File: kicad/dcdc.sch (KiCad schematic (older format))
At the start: 48 parts, among them Q1 IPP045N10N3G, Q2 IPP045N10N3G, Q3 IPP045N10N3G, U1 LM5107, U3 INA186

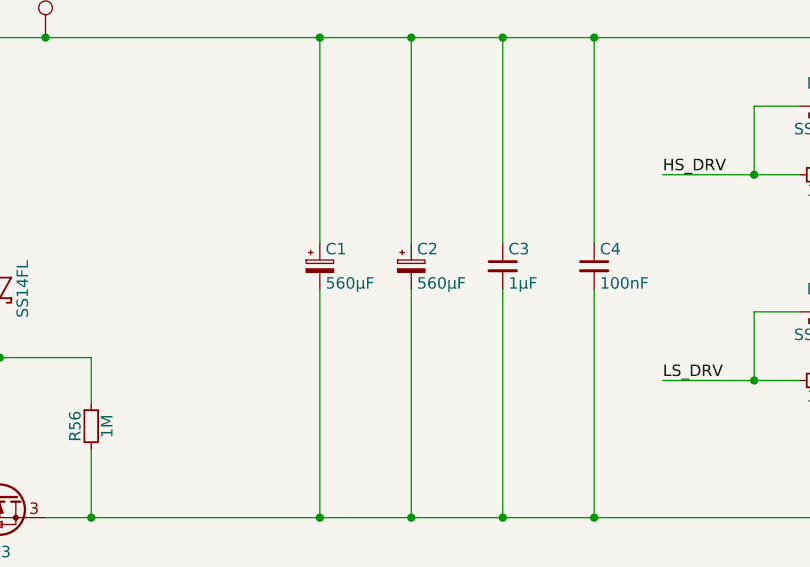
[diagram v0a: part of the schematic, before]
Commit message: Small updates in layout and documentation (v0.1.1)
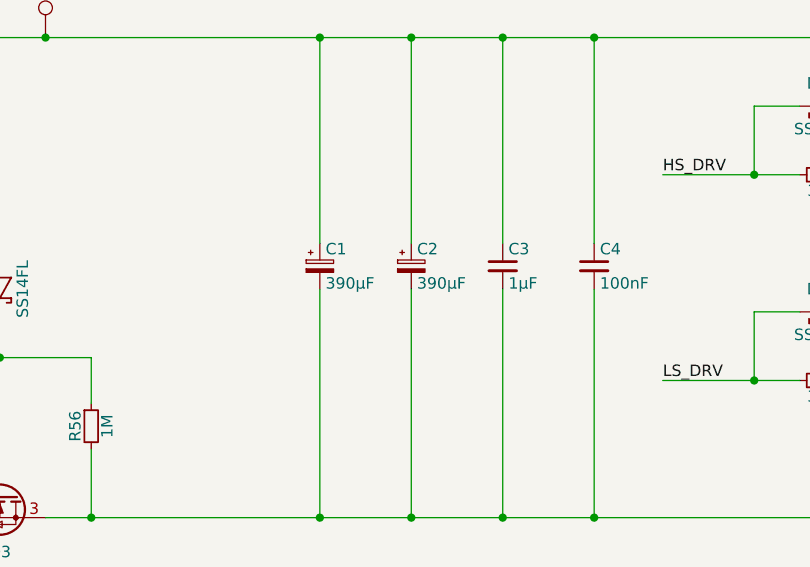
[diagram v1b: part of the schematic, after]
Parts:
- C1, C2: value 560µF -> 390µF; PartNumber EKZN101ELL561MM25S -> EKZN101ELL391MM20S; Remarks 100V, 2.27A, 18x25 -> 100V, 2.27A, 18x20
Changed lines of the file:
@@
 Sheet 2 6
 Title "MPPT 2420 HC"
-Date "2020-05-08"
-Rev "0.1"
+Date "2020-11-18"
+Rev "0.1.1"
 Comp "Libre Solar Technologies GmbH"
 Comment1 "Author: Martin Jäger"
@@
 P 4700 2500
 F 0 "C2" H 4725 2575 50  0000 L CNN
-F 1 "560µF" H 4725 2425 50  0000 L CNN
+F 1 "390µF" H 4725 2425 50  0000 L CNN
 F 2 "Capacitor_THT:CP_Radial_D18.0mm_P7.50mm" H 4725 2275 50  0001 L CNN
 F 3 "" H 4725 2575 50  0000 C CNN
 F 4 "United Chemi-Con" H 1300 700 50  0001 C CNN "Manufacturer"
-F 5 "EKZN101ELL561MM25S" H 1300 700 50  0001 C CNN "PartNumber"
-F 6 "100V, 2.27A, 18x25" H 700 400 60  0001 C CNN "Remarks"
+F 5 "EKZN101ELL391MM20S" H 1300 700 50  0001 C CNN "PartNumber"
+F 6 "100V, 2.27A, 18x20" H 700 400 60  0001 C CNN "Remarks"
 	1    4700 2500
 	1    0    0    -1
@@
 P 4300 2500
 F 0 "C1" H 4325 2575 50  0000 L CNN
-F 1 "560µF" H 4325 2425 50  0000 L CNN
+F 1 "390µF" H 4325 2425 50  0000 L CNN
 F 2 "Capacitor_THT:CP_Radial_D18.0mm_P7.50mm" H 4325 2275 50  0001 L CNN
 F 3 "" H 4325 2575 50  0000 C CNN
 F 4 "United Chemi-Con" H 900 700 50  0001 C CNN "Manufacturer"
-F 5 "EKZN101ELL561MM25S" H 900 700 50  0001 C CNN "PartNumber"
-F 6 "100V, 2.27A, 18x25" H 700 400 60  0001 C CNN "Remarks"
+F 5 "EKZN101ELL391MM20S" H 900 700 50  0001 C CNN "PartNumber"
+F 6 "100V, 2.27A, 18x20" H 700 400 60  0001 C CNN "Remarks"
 	1    4300 2500
 	1    0    0    -1

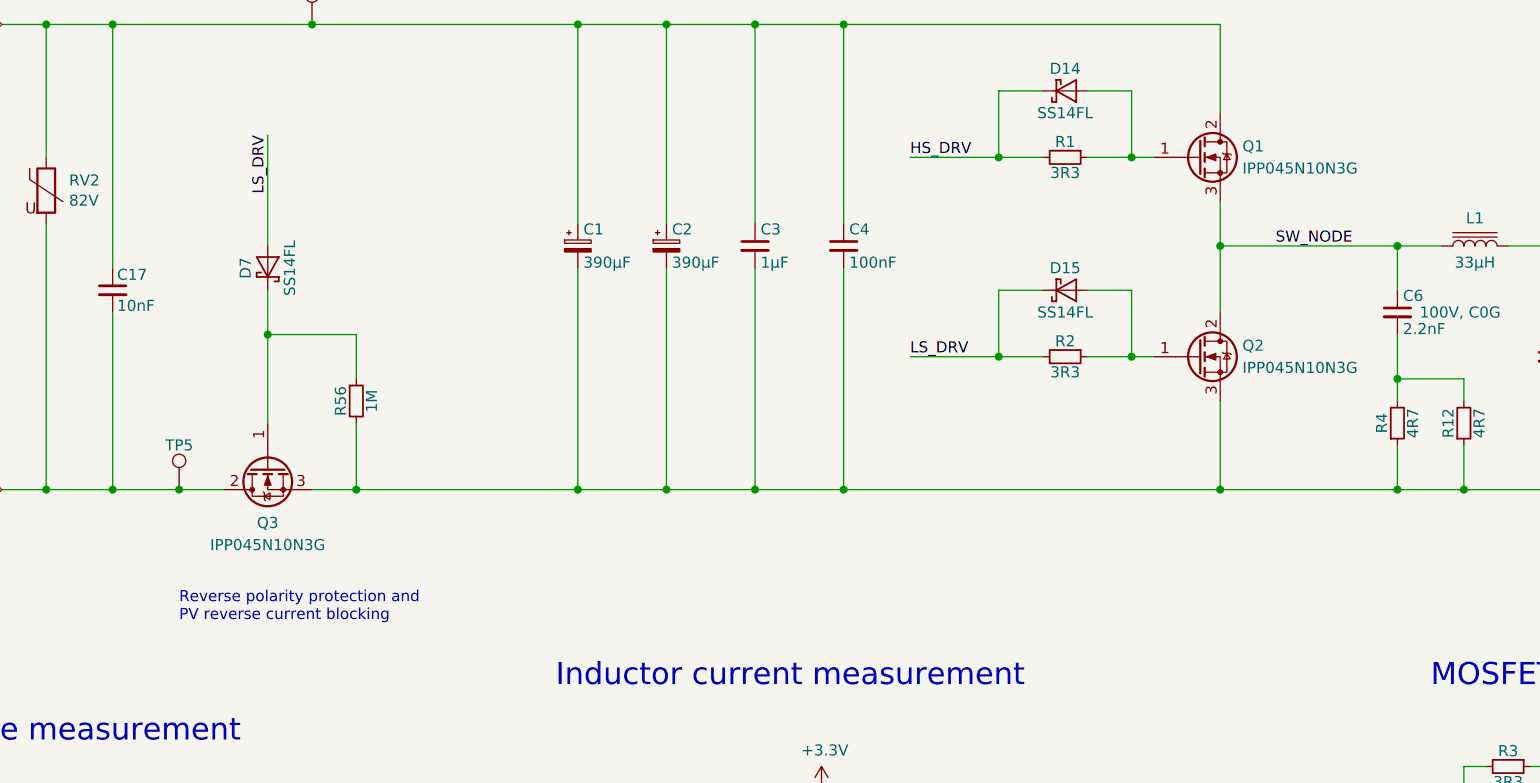
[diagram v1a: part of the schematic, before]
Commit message: Update to v0.2 with improvements after testing
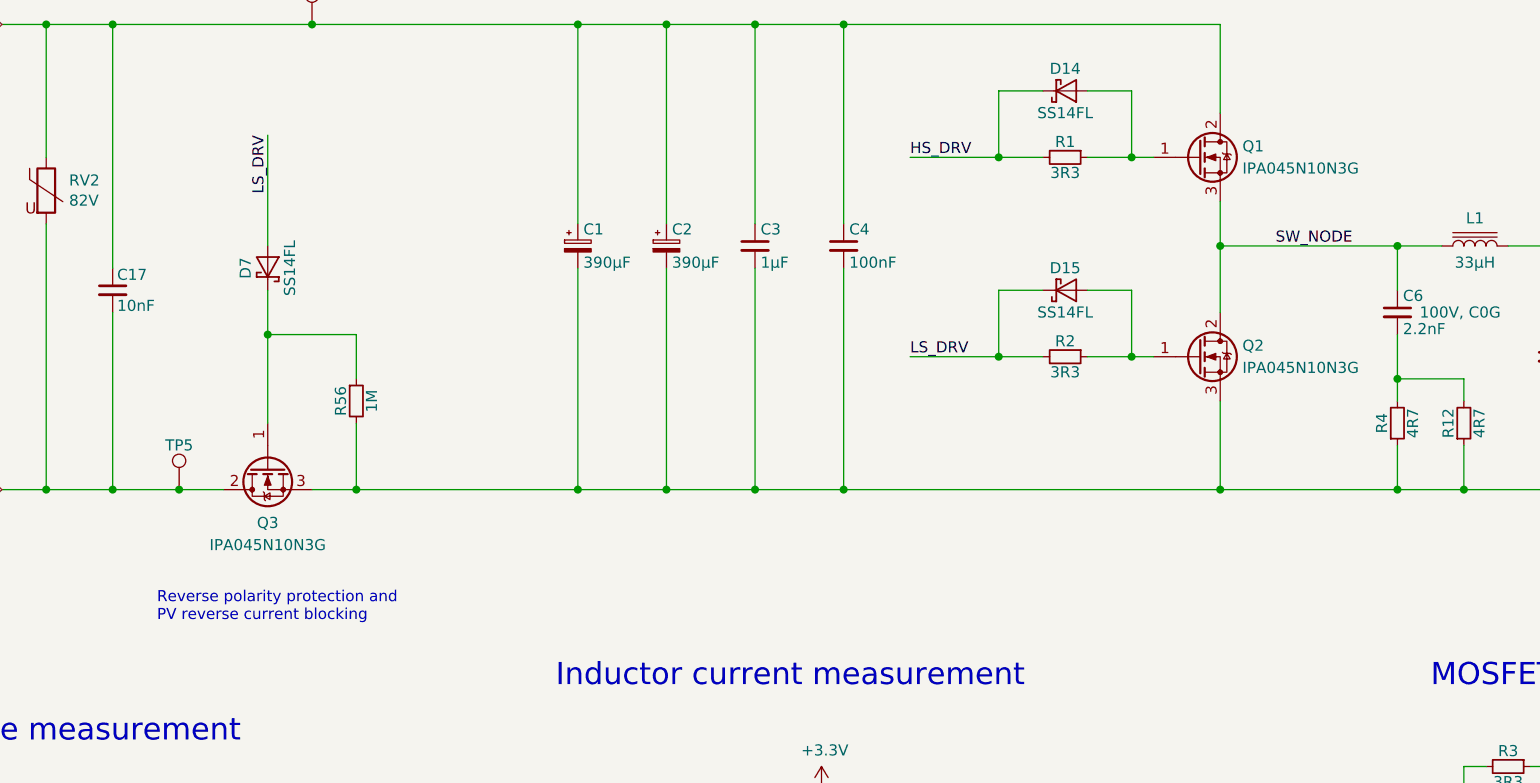
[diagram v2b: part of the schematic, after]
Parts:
- C42, C44: Manufacturer (none) -> EPCOS / TDK; PartNumber 224J63 -> B32529C224J; Remarks (none) -> Alternative: Kemet MMK5224K63J01L16.5TA18
- Q1, Q2, Q3: value IPP045N10N3G -> IPA045N10N3G; PartNumber IPP045N10N3G -> IPA045N10N3G; Remarks Alternative: IPA045N10N3G -> Alternative: IPP045N10N3G
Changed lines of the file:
@@
 Sheet 2 6
 Title "MPPT 2420 HC"
-Date "2020-11-18"
-Rev "0.1.1"
+Date "2020-12-11"
+Rev "0.2"
 Comp "Libre Solar Technologies GmbH"
-Comment1 "Author: Martin Jäger"
-Comment2 "Website: http://libre.solar"
-Comment3 ""
+Comment1 "https://libre.solar"
+Comment2 "Author: Martin Jäger"
+Comment3 "License: Creative Commons Attribution-ShareAlike 4.0 International"
 Comment4 ""
 $EndDescr
@@
 P 7100 2100
 F 0 "Q1" H 7300 2150 50  0000 L CNN
-F 1 "IPP045N10N3G" H 7300 2050 50  0000 L CNN
+F 1 "IPA045N10N3G" H 7300 2050 50  0000 L CNN
 F 2 "LibreSolar:TO-220-3_Horizontal_BottomHeatsink" H 7300 2200 50  0001 C CNN
 F 3 "" H 7100 2100 50  0001 C CNN
 F 4 "Infineon" H 1100 300 50  0001 C CNN "Manufacturer"
-F 5 "IPP045N10N3G" H 1100 300 50  0001 C CNN "PartNumber"
+F 5 "IPA045N10N3G" H 1100 300 50  0001 C CNN "PartNumber"
 F 6 "" H 7100 2100 50  0001 C CNN "Alternative"
-F 7 "Alternative: IPA045N10N3G" H 7100 2100 50  0001 C CNN "Remarks"
+F 7 "Alternative: IPP045N10N3G" H 7100 2100 50  0001 C CNN "Remarks"
 	1    7100 2100
 	1    0    0    -1
@@
 P 7100 3000
 F 0 "Q2" H 7300 3050 50  0000 L CNN
-F 1 "IPP045N10N3G" H 7300 2950 50  0000 L CNN
+F 1 "IPA045N10N3G" H 7300 2950 50  0000 L CNN
 F 2 "LibreSolar:TO-220-3_Horizontal_BottomHeatsink" H 7300 3100 50  0001 C CNN
 F 3 "" H 7100 3000 50  0001 C CNN
 F 4 "Infineon" H 1100 500 50  0001 C CNN "Manufacturer"
-F 5 "IPP045N10N3G" H 1100 500 50  0001 C CNN "PartNumber"
+F 5 "IPA045N10N3G" H 1100 500 50  0001 C CNN "PartNumber"
 F 6 "" H 7100 3000 50  0001 C CNN "Alternative"
-F 7 "Alternative: IPA045N10N3G" H 7100 3000 50  0001 C CNN "Remarks"
+F 7 "Alternative: IPP045N10N3G" H 7100 3000 50  0001 C CNN "Remarks"
 	1    7100 3000
 	1    0    0    -1
@@
 	2200 2800 2200 3600
 Connection ~ 2200 3600
-Text Notes 2500 4200 0    50   ~ 0
+Text Notes 2400 4200 0    50   ~ 0
 Reverse polarity protection and\nPV reverse current blocking
 Wire Wire Line
@@
 F 2 "Capacitor_THT:C_Rect_L7.2mm_W3.5mm_P5.00mm_FKS2_FKP2_MKS2_MKP2" H 8700 2800 50  0001 C CNN
 F 3 "" H 8725 3075 50  0001 C CNN
-F 4 "224J63" H 8700 3000 50  0001 C CNN "PartNumber"
+F 4 "B32529C224J" H 8700 3000 50  0001 C CNN "PartNumber"
+F 5 "EPCOS / TDK" H 8700 3000 50  0001 C CNN "Manufacturer"
+F 6 "Alternative: Kemet MMK5224K63J01L16.5TA18" H 8700 3000 50  0001 C CNN "Remarks"
 	1    8700 3000
 	1    0    0    -1
@@
 F 2 "Capacitor_THT:C_Rect_L7.2mm_W3.5mm_P5.00mm_FKS2_FKP2_MKS2_MKP2" H 9300 2800 50  0001 C CNN
 F 3 "" H 9325 3075 50  0001 C CNN
-F 4 "224J63" H 9300 3000 50  0001 C CNN "PartNumber"
+F 4 "B32529C224J" H 9300 3000 50  0001 C CNN "PartNumber"
+F 5 "EPCOS / TDK" H 9300 3000 50  0001 C CNN "Manufacturer"
+F 6 "Alternative: Kemet MMK5224K63J01L16.5TA18" H 9300 3000 50  0001 C CNN "Remarks"
 	1    9300 3000
 	-1   0    0    1
@@
 AR Path="/5C5B9319/5DBB6507" Ref="Q?"  Part="1"
 F 0 "Q3" V 3150 3500 50  0000 C CNN
-F 1 "IPP045N10N3G" V 3250 3500 50  0000 C CNN
+F 1 "IPA045N10N3G" V 3250 3500 50  0000 C CNN
 F 2 "LibreSolar:TO-220-3_Horizontal_BottomHeatsink" H 3100 3600 50  0001 C CNN
 F 3 "" H 2900 3500 50  0001 C CNN
 F 4 "Infineon" H 300 1050 50  0001 C CNN "Manufacturer"
-F 5 "Alternative: IPA045N10N3G" H 2900 3500 50  0001 C CNN "Remarks"
-F 6 "IPP045N10N3G" H 2900 3500 50  0001 C CNN "PartNumber"
+F 5 "Alternative: IPP045N10N3G" H 2900 3500 50  0001 C CNN "Remarks"
+F 6 "IPA045N10N3G" H 2900 3500 50  0001 C CNN "PartNumber"
 	1    2900 3500
 	0    -1   1    0

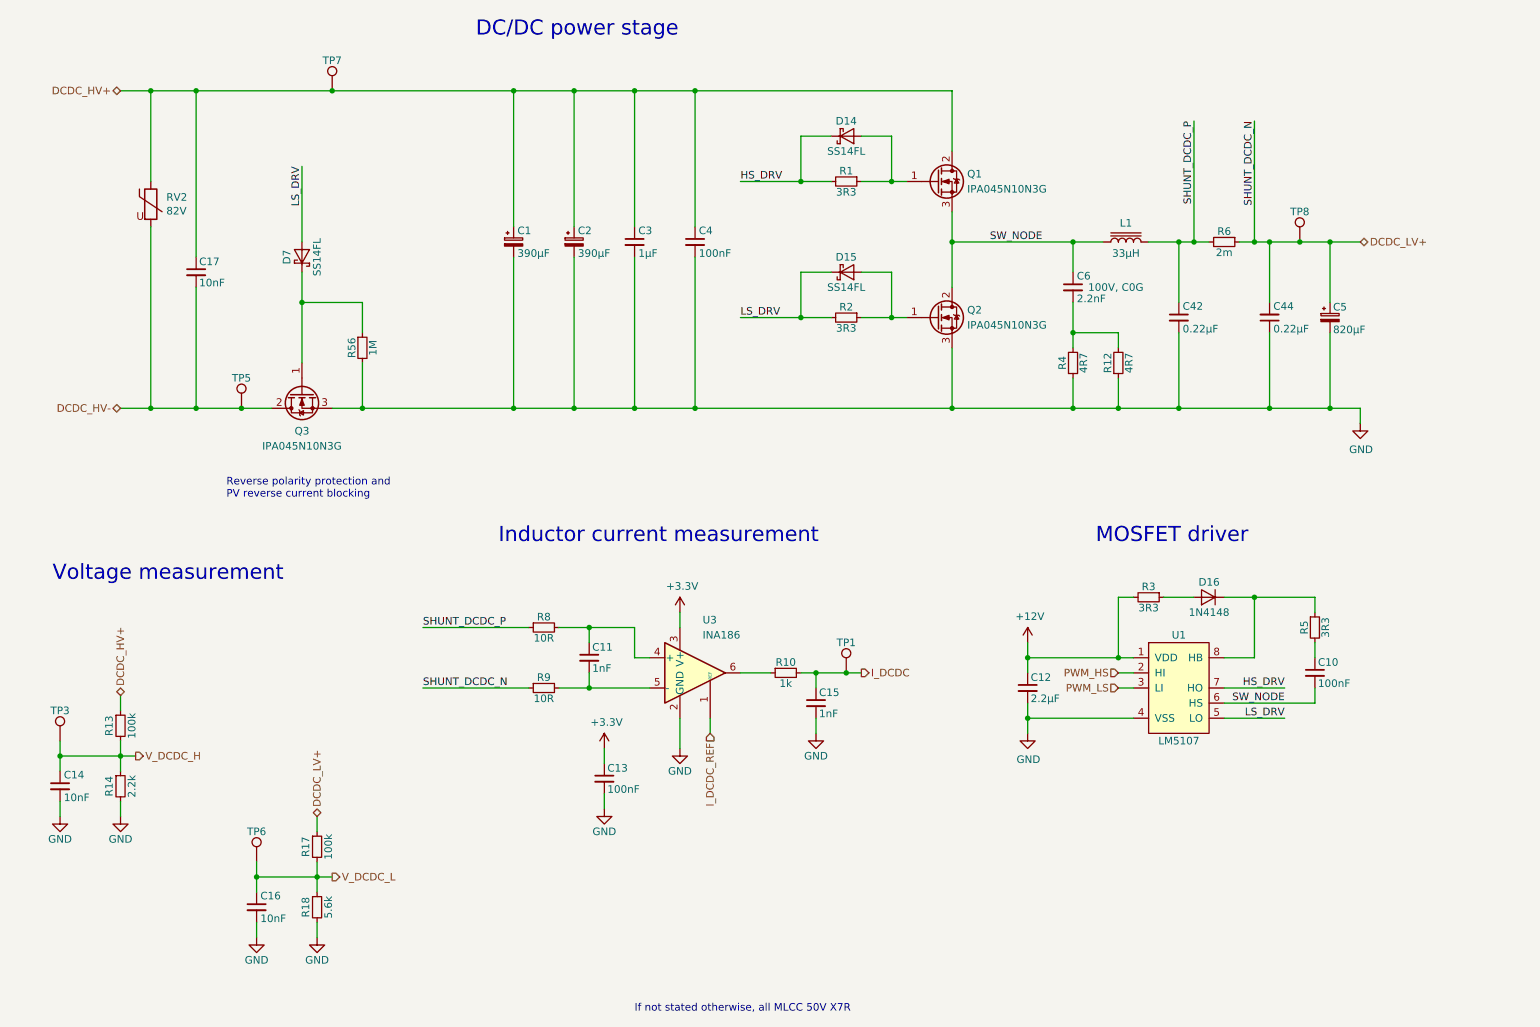
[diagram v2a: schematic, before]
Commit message: Minor updates for v0.2.1
Adjustments in silk screen and second bulk output cap.
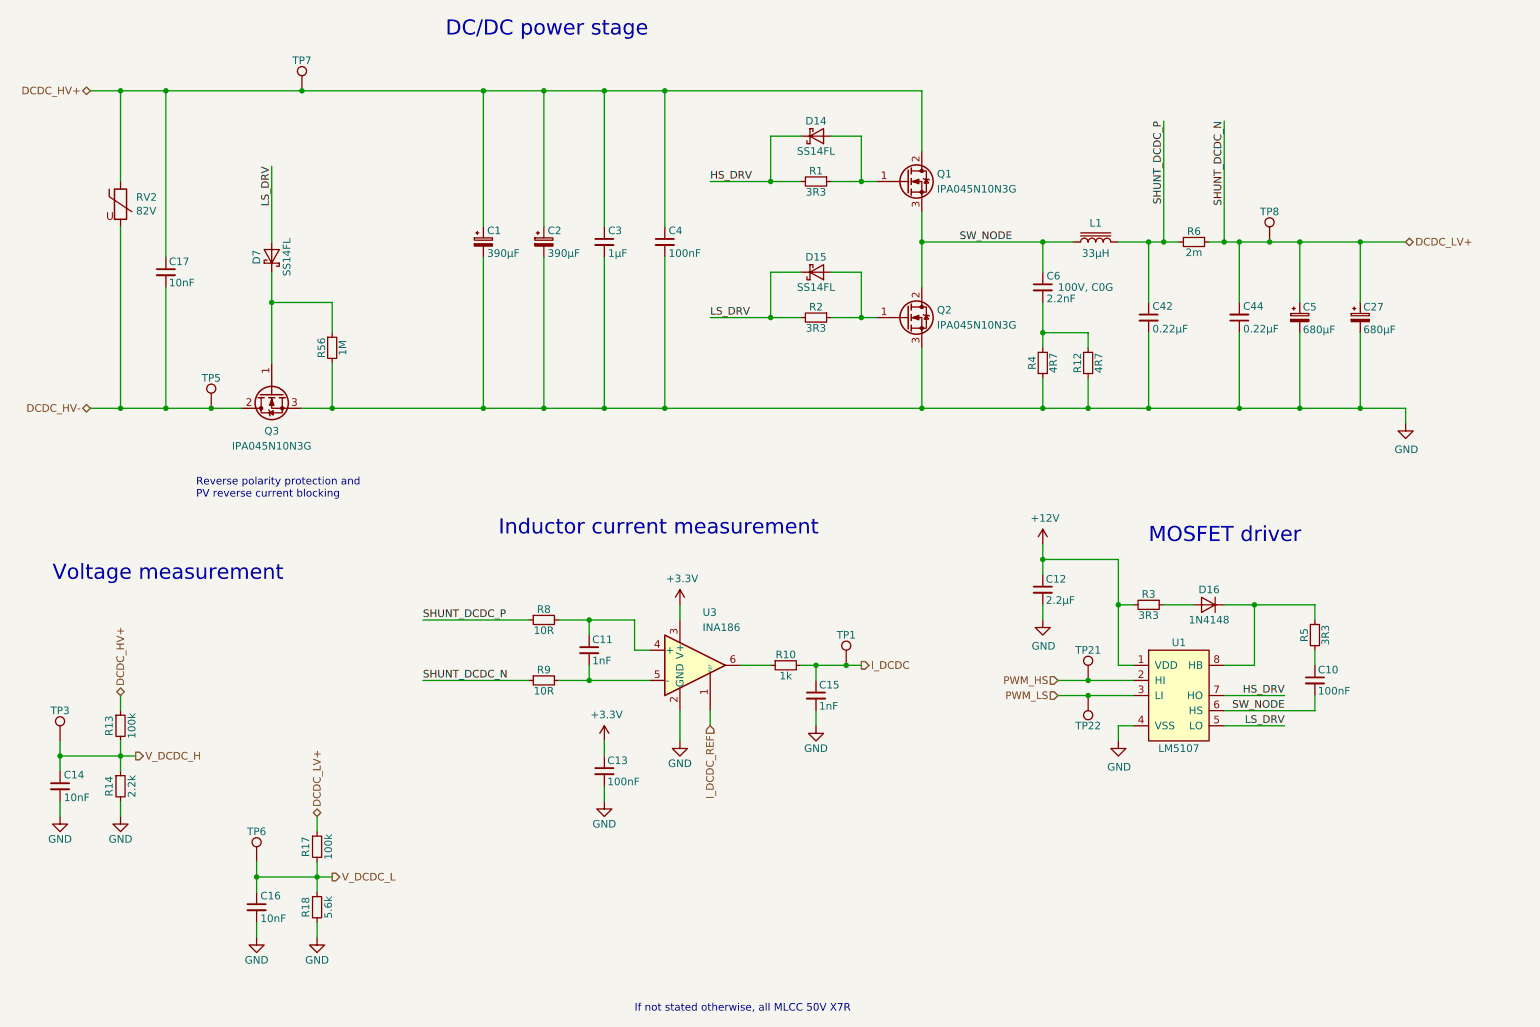
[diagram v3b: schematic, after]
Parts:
- added C27: 680µF, Capacitor_THT:CP_Radial_D10.0mm_P5.00mm, symbol Device:CP_Small
- added TP21, TP22: 1.5mm, TestPoint:TestPoint_Pad_D1.5mm, symbol Connector:TestPoint
- C5: value 820µF -> 680µF; PartNumber EEU-FR1V821L -> EEU-FR1V681; Remarks 35V, 2.47A -> 35V, 2.18A, 10x20
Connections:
- net DCDC_LV+: now also C27.1
- net GND: now also C27.2
- net PWM_HS: now also TP21.1
- net PWM_LS: now also TP22.1
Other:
- moved on the sheet: C1, C10, C11, C12, C13, C15, C17, C2, C3, C4, C42, C44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
